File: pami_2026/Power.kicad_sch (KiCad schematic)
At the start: 30 parts, among them J1 Conn_01x02_Pin, Q1 PMOS, U2 AP63205WU, U3 DRV8838, U4 DRV8838, U5 AP63203WU

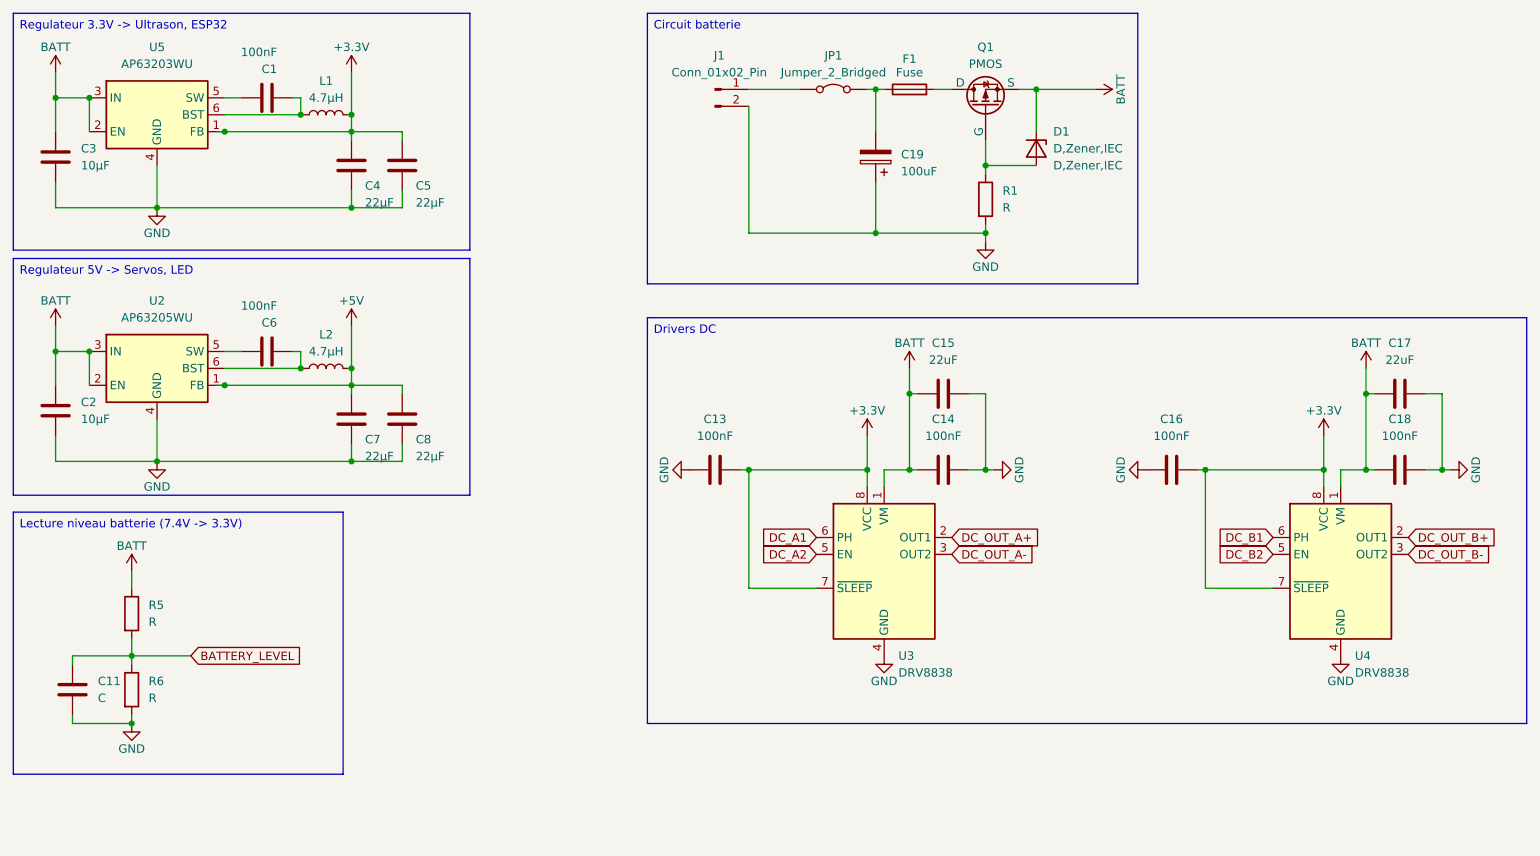
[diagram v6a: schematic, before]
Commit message: Ultrason, empreintes et petites corrections
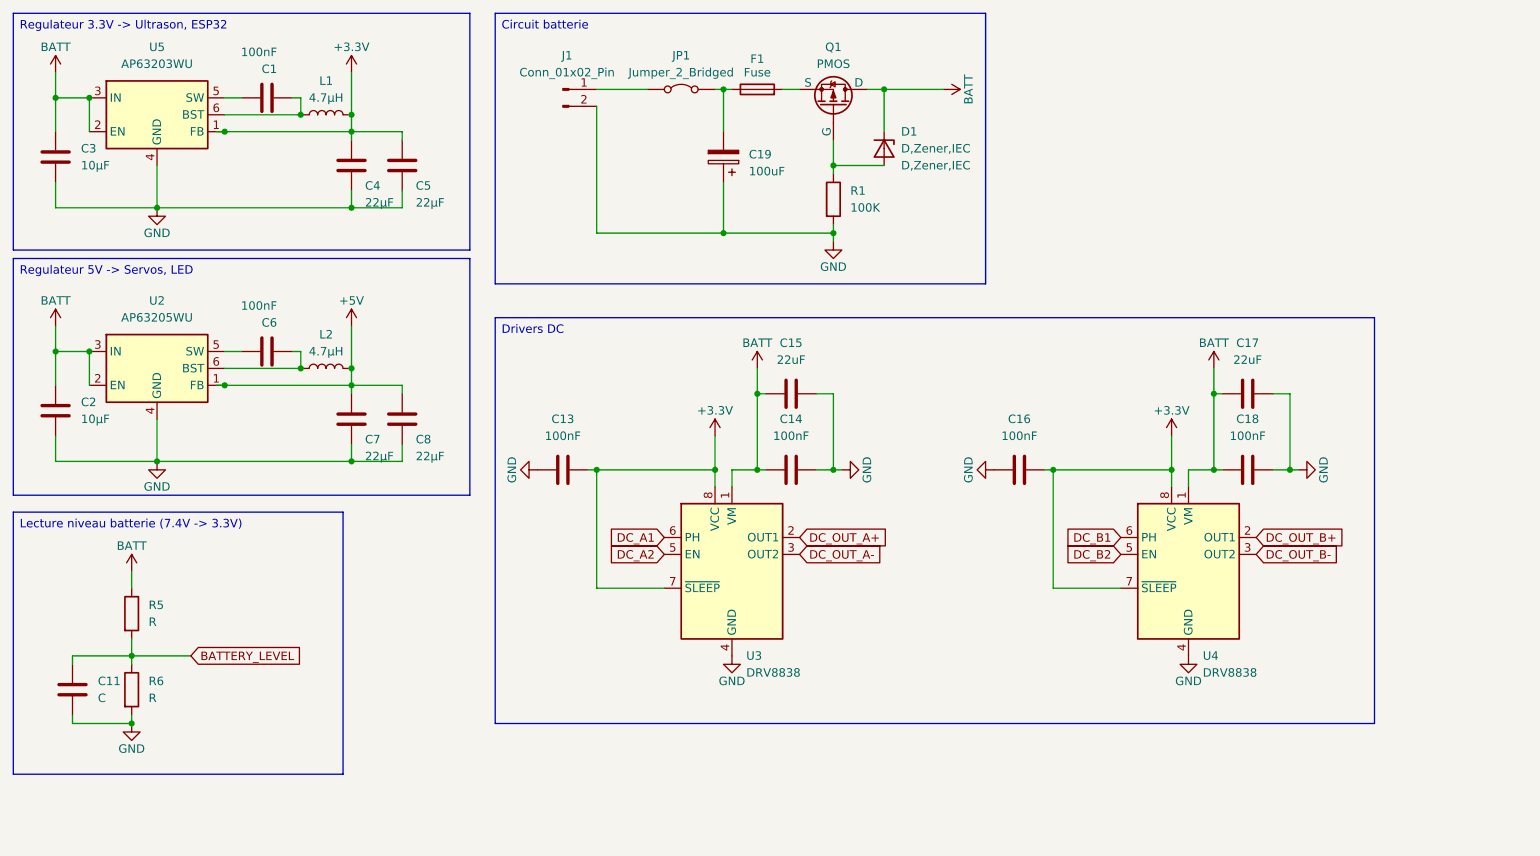
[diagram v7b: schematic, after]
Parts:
- C1, C6: footprint Capacitor_SMD:C_0201_0603Metric -> Capacitor_SMD:C_0603_1608Metric
- C11, C13, C14, C16, C18, C19: footprint (none) -> Capacitor_SMD:C_0603_1608Metric
- C15, C17: footprint (none) -> Capacitor_SMD:C_0805_2012Metric
- C2, C3, C4, C5, C7, C8: footprint Capacitor_SMD:C_0201_0603Metric -> Capacitor_SMD:C_0805_2012Metric
- D1: footprint (none) -> Diode_SMD:D_SOD-123
- F1: footprint (none) -> Fuse:Fuse_1206_3216Metric
- J1: footprint (none) -> Connector_PinHeader_2.54mm:PinHeader_1x01_P2.54mm_Vertical
- JP1: footprint (none) -> Jumper:SolderJumper-2_P1.3mm_Bridged_RoundedPad1.0x1.5mm
- Q1: footprint (none) -> Package_TO_SOT_SMD:SOT-223
- R1: value R -> 100K; footprint Resistor_SMD:R_0201_0603Metric -> Resistor_SMD:R_0603_1608Metric
- R5, R6: footprint (none) -> Resistor_SMD:R_0603_1608Metric
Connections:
- net BATT: now also Q1.1 (D); no longer Q1.3 (S)
- net at F1.2: now also Q1.3 (S); no longer Q1.1 (D)
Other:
- moved on the sheet: C13, C14, C15, C16, C17, C18, C19, D1, F1, J1, JP1, Q1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

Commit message: Fix polarity protection and change drivers
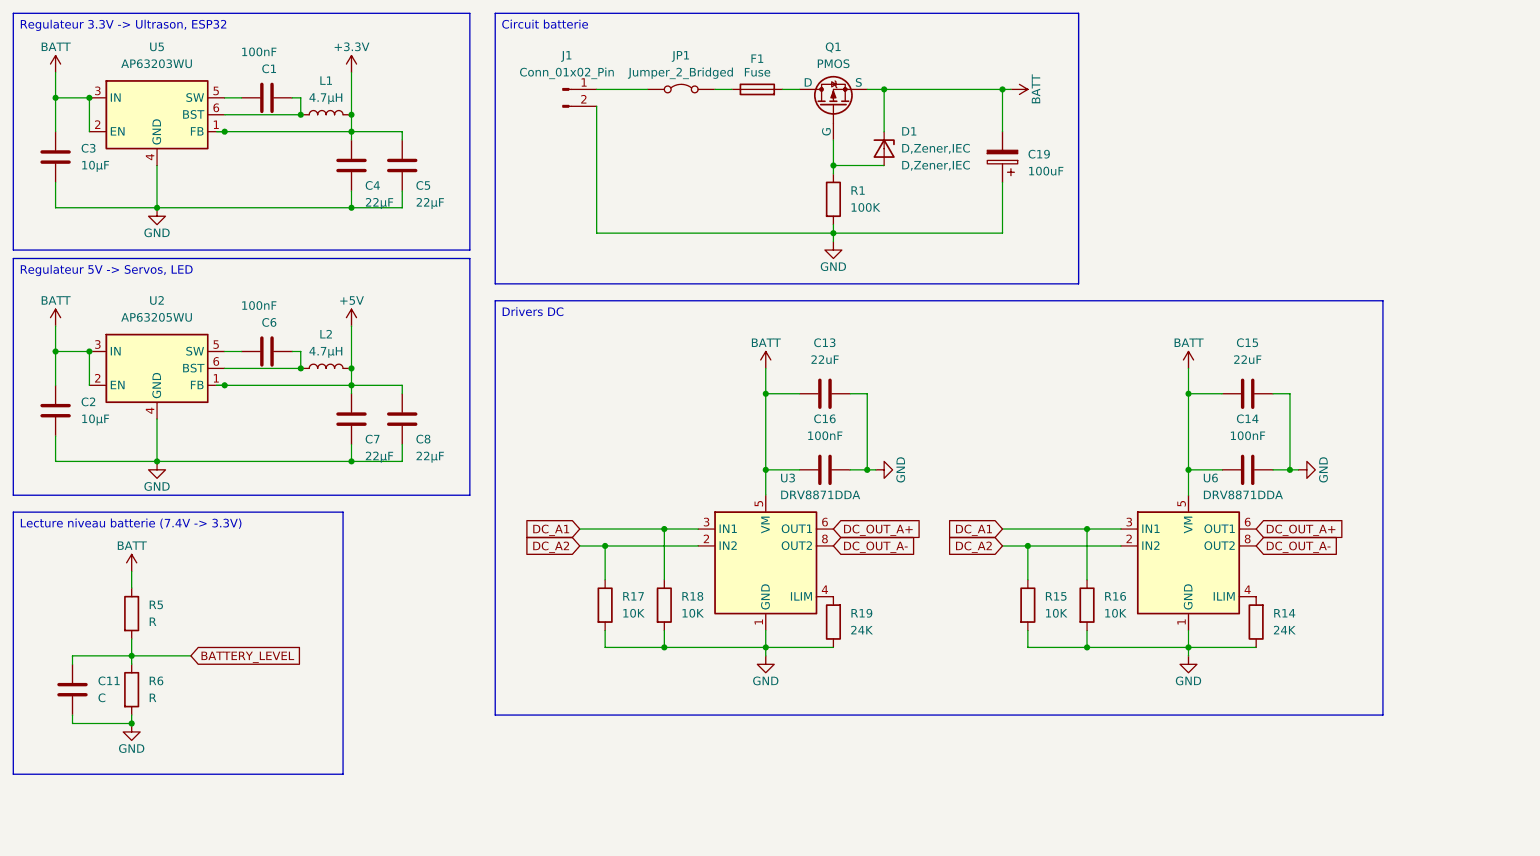
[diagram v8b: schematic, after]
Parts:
- removed C17: 22uF, Capacitor_SMD:C_0805_2012Metric, symbol Device:C
- removed C18: 100nF, Capacitor_SMD:C_0603_1608Metric, symbol Device:C
- removed U3, U4: DRV8838, Package_SON:WSON-8-1EP_2x2mm_P0.5mm_EP0.9x1.6mm, symbol Driver_Motor:DRV8838
- added R14, R19: 24K, symbol Device:R
- added R15, R16, R17, R18: 10K, symbol Device:R
- added U3, U6: DRV8871DDA, Package_SO:Texas_HTSOP-8-1EP_3.9x4.9mm_P1.27mm_EP2.95x4.9mm_Mask2.4x3.1mm_ThermalVias, symbol Driver_Motor:DRV8871DDA
- C13: value 100nF -> 22uF; footprint Capacitor_SMD:C_0603_1608Metric -> Capacitor_SMD:C_0805_2012Metric
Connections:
- net +3.3V: no longer C13.2, C16.2
- net BATT: now also C13.1, C16.1, C19.2, Q1.3 (S), U3.5 (VM), U6.5 (VM); no longer Q1.1 (D)
- net DC_A1: now also R16.1, R18.1, U3.3 (IN1), U6.3 (IN1)
- net DC_A2: now also R15.1, R17.1, U3.2 (IN2), U6.2 (IN2)
- net DC_OUT_A+: now also U3.6 (OUT1), U6.6 (OUT1)
- net DC_OUT_A-: now also U3.8 (OUT2), U6.8 (OUT2)
- net GND: now also C13.2, C16.2, R14.1, R15.2, R16.2, R17.2, R18.2, R19.1, U3.1 (GND), U3.7 (GND), U3.9 (GND), U6.1 (GND), U6.7 (GND), U6.9 (GND); no longer C13.1, C16.1
- net at F1.2: now also Q1.1 (D); no longer Q1.3 (S)
- net at F1.1, JP1.2 (B): no longer C19.2
- new net: R19.2, U3.4 (ILIM)
- new net: R14.2, U6.4 (ILIM)
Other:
- moved on the sheet: C14, C15, C19, Q1
